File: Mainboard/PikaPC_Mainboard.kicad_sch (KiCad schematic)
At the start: 60 parts, among them J1 Conn_02x20_Odd_Even, J10 Conn_01x08, J11 Conn_01x08, J12 Conn_01x08, J13 Conn_01x08, J14 Conn_01x08, J15 Conn_01x08, J16 Conn_01x08, J17 Conn_01x08, J18 Conn_01x10, J19 Conn_02x05_Odd_Even, J2 Conn_02x20_Odd_Even, J3 Conn_02x20_Odd_Even, J4 Conn_02x20_Odd_Even, J5 Conn_01x18, J6 Conn_01x18, J7 Conn_01x18, J8 Conn_01x18, J9 Conn_01x08, SW1 SW_Push_DPDT, SW2 SW_Push, U1 PPC403GA, U10 74LVC245, U11 74LVC245, U12 GD75232N, U13 74LVC125, U14 MCP120-315GI/TO, U2 TE-822021-4, U3 SST39VF010, U4 74HCT244, U5 74HCT244, U6 74HCT244, U7 74LVC245, U8 74HCT32, U9 74LVC245, Y1 25M, Y2 7M3728

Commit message: Change from 72-pin SIMM to SRAM
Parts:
- removed J5, J6, J7, J8: Conn_01x18, Connector_PinHeader_2.54mm:PinHeader_1x18_P2.54mm_Vertical, symbol Connector_Generic:Conn_01x18
- removed U10, U11, U7, U9: 74LVC245, Package_DIP:DIP-20_W7.62mm_Socket, symbol 74xx:74HC245
- removed U2: TE-822021-4, PikaPC:SIMM72, symbol PikaPC:SIMM72
- removed U4, U5, U6: 74HCT244, Package_DIP:DIP-20_W7.62mm_Socket, symbol 74xx:74HCT244
- removed U8: 74HCT32, Package_DIP:DIP-14_W7.62mm_Socket, symbol 74xx:74LS32
- added C17, C18: 100nF, Capacitor_THT:C_Disc_D3.0mm_W2.0mm_P2.50mm, symbol Device:C_Small_US
- added U15, U16: AS6C4008-55PCN, Package_DIP:DIP-32_W15.24mm, symbol Memory_RAM:AS6C4008-55PCN
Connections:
- net +3.3V: now also C17.1, C18.1, U15.32 (VCC), U16.32 (VCC)
- net A1: now also U15.12 (A0), U16.12 (A0)
- net A10: now also U15.26 (A9), U16.26 (A9)
- net A11: now also U15.23 (A10), U16.23 (A10)
- net A12: now also U15.25 (A11), U16.25 (A11)
- net A13: now also U15.4 (A12), U16.4 (A12)
- net A14: now also U15.28 (A13), U16.28 (A13)
- net A15: now also U15.3 (A14), U16.3 (A14)
- net A16: now also U15.31 (A15), U16.31 (A15)
- net A17: now also U15.2 (A16), U16.2 (A16)
- net A18: now also U15.30 (A17), U16.30 (A17)
- net A19: now also U15.1 (A18), U16.1 (A18)
- net A2: now also U15.11 (A1), U16.11 (A1)
- net A26: no longer U1.123 (~{WBE1}/A5)
- net A27: no longer U1.122 (~{WBE0}/A4)
- net A3: now also U15.10 (A2), U16.10 (A2)
- net A4: now also U15.9 (A3), U16.9 (A3)
- net A5: now also U15.8 (A4), U16.8 (A4)
- net A6: now also U15.7 (A5), U16.7 (A5)
- net A7: now also U15.6 (A6), U16.6 (A6)
- net A8: now also U15.5 (A7), U16.5 (A7)
- net A9: now also U15.27 (A8), U16.27 (A8)
- net D16: now also U15.13 (DQ0)
- net D17: now also U15.14 (DQ1)
- net D18: now also U15.15 (DQ2)
- net D19: now also U15.17 (DQ3)
- net D20: now also U15.18 (DQ4)
- net D21: now also U15.19 (DQ5)
- net D22: now also U15.20 (DQ6)
- net D23: now also U15.21 (DQ7)
- net D24: now also U16.13 (DQ0)
- net D25: now also U16.14 (DQ1)
- net D26: now also U16.15 (DQ2)
- net D27: now also U16.17 (DQ3)
- net D28: now also U16.18 (DQ4)
- net D29: now also U16.19 (DQ5)
- net D30: now also U16.20 (DQ6)
- net D31: now also U16.21 (DQ7)
- net GND: now also C17.2, C18.2, U15.16 (VSS), U16.16 (VSS)
- net ~{CS1}: now also U15.22 (CE#), U16.22 (CE#)
- net ~{OE}: now also U15.24 (OE#), U16.24 (OE#)
- new net ~{WBE0}: U1.122 (~{WBE0}/A4), U16.29 (WE#)
- new net ~{WBE1}: U1.123 (~{WBE1}/A5), U15.29 (WE#)
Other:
- moved on the sheet: C13, C14, U13E, U3

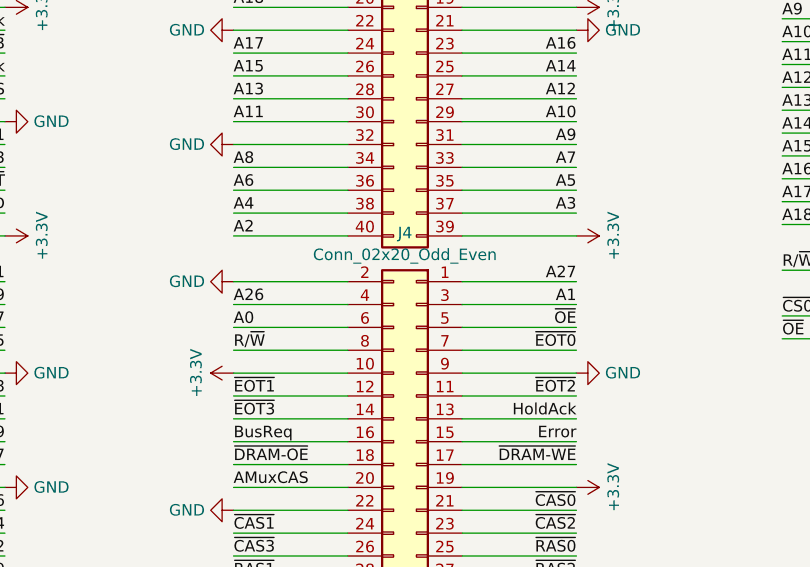
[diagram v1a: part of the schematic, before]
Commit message: Rename write strobes
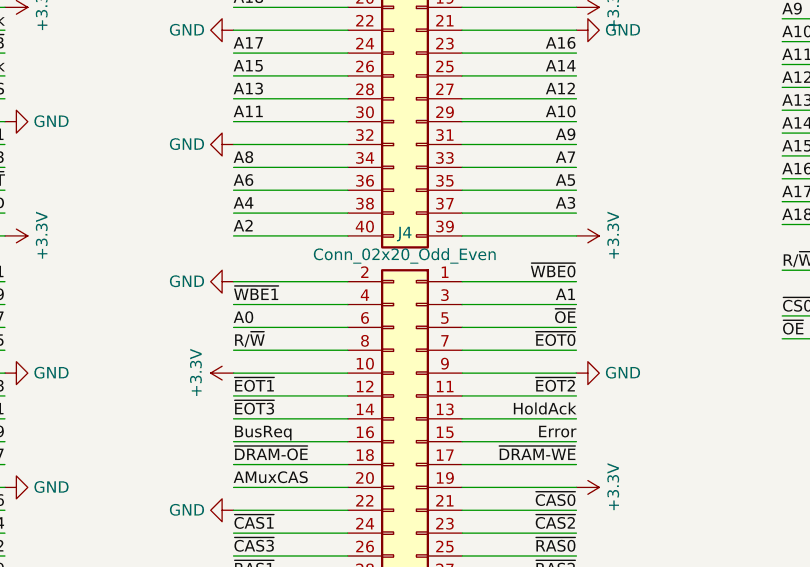
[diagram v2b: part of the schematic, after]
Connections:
- net A26 is gone; now on net ~{WBE1}: J4.4 (Pin_4)
- net A27 is gone; now on net ~{WBE0}: J4.1 (Pin_1)
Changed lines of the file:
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@@
 		)
 	)
-	(label "A26"
+	(label "~{WBE1}"
 		(at 292.1 81.28 0)
 		(effects
@@
 		)
 	)
-	(label "A27"
+	(label "~{WBE0}"
 		(at 330.2 78.74 180)
 		(effects

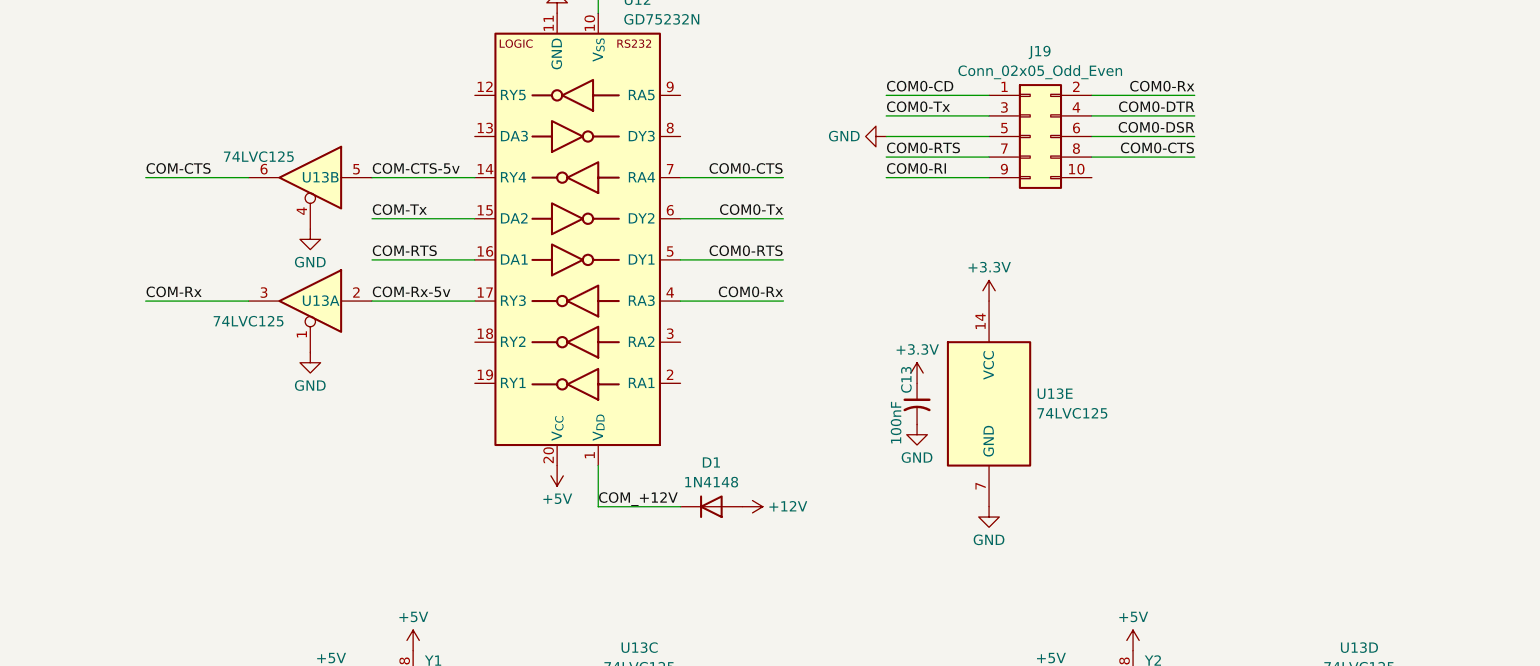
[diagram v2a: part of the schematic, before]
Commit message: use 5V signalling for Rx & CTS
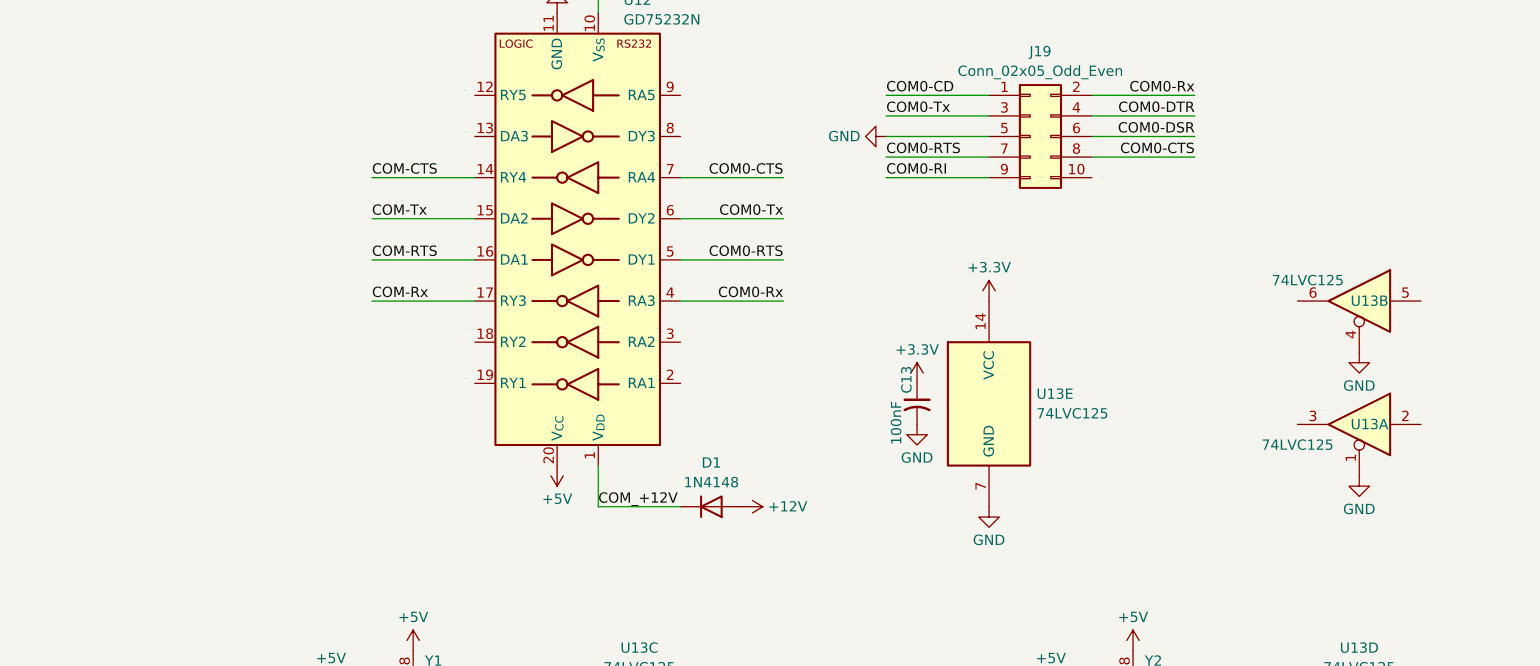
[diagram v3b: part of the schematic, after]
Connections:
- net COM-CTS: now also U12.14 (RY4); no longer U13.6
- net COM-Rx: now also U12.17 (RY3); no longer U13.3
- net COM-CTS-5v: no longer names the net of U13.5
- net COM-CTS-5v: no longer U12.14 (RY4)
- net COM-Rx-5v: no longer names the net of U13.2
- net COM-Rx-5v: no longer U12.17 (RY3)
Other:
- moved on the sheet: U13A, U13B
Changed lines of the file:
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@@
 	(wire
 		(pts
-			(xy 457.2 -101.6) (xy 469.9 -101.6)
-		)
-		(stroke
-			(width 0)
-			(type default)
-		)
-	)
-	(wire
-		(pts
 			(xy 495.3 44.45) (xy 482.6 44.45)
 		)
@@
 	(wire
 		(pts
-			(xy 457.2 -116.84) (xy 469.9 -116.84)
-		)
-		(stroke
-			(width 0)
-			(type default)
-		)
-	)
-	(wire
-		(pts
 			(xy 149.86 228.6) (xy 152.4 228.6)
 		)
@@
 	(wire
 		(pts
-			(xy 441.96 -101.6) (xy 429.26 -101.6)
+			(xy 469.9 -101.6) (xy 457.2 -101.6)
 		)
 		(stroke
@@
 	(wire
 		(pts
-			(xy 441.96 -116.84) (xy 429.26 -116.84)
+			(xy 469.9 -116.84) (xy 457.2 -116.84)
 		)
 		(stroke
@@
 		)
 	)
-	(label "COM-CTS-5v"
-		(at 457.2 -116.84 0)
-		(effects
-			(font
-				(size 1.27 1.27)
-			)
-			(justify left bottom)
-		)
-	)
 	(label "BusReq"
 		(at 205.74 55.88 180)
@@
 		)
 	)
-	(label "COM-Rx-5v"
-		(at 457.2 -101.6 0)
-		(effects
-			(font
-				(size 1.27 1.27)
-			)
-			(justify left bottom)
-		)
-	)
 	(label "A1"
 		(at 330.2 81.28 180)
@@
 	)
 	(label "COM-Rx"
-		(at 429.26 -101.6 0)
+		(at 457.2 -101.6 0)
 		(effects
 			(font
@@
 	)
 	(label "COM-CTS"
-		(at 429.26 -116.84 0)
+		(at 457.2 -116.84 0)
 		(effects
 			(font
@@
 	(symbol
 		(lib_id "power:GND")
-		(at 449.58 -110.49 0)
+		(at 579.12 -95.25 0)
 		(unit 1)
 		(exclude_from_sim no)
@@
 		(dnp no)
 		(property "Reference" "#PWR069"
-			(at 449.58 -104.14 0)
+			(at 579.12 -88.9 0)
 			(effects
 				(font
@@
 		)
 		(property "Value" "GND"
-			(at 449.58 -106.3569 0)
+			(at 579.12 -91.1169 0)
 			(effects
 				(font
@@
 		)
 		(property "Footprint" ""
-			(at 449.58 -110.49 0)
+			(at 579.12 -95.25 0)
 			(effects
 				(font
@@
 		)
 		(property "Datasheet" ""
-			(at 449.58 -110.49 0)
+			(at 579.12 -95.25 0)
 			(effects
 				(font
@@
 		)
 		(property "Description" "Power symbol creates a global label with name \"GND\" , ground"
-			(at 449.58 -110.49 0)
+			(at 579.12 -95.25 0)
 			(effects
 				(font
@@
 	(symbol
 		(lib_id "74xx:74LVC125")
-		(at 449.58 -116.84 0)
+		(at 579.12 -101.6 0)
 		(mirror y)
 		(unit 2)
@@
 		(dnp no)
 		(property "Reference" "U13"
-			(at 450.85 -116.84 0)
+			(at 580.39 -101.6 0)
 			(effects
 				(font
@@
 		)
 		(property "Value" "74LVC125"
-			(at 443.23 -119.38 0)
+			(at 572.77 -104.14 0)
 			(effects
 				(font
@@
 		)
 		(property "Footprint" "Package_DIP:DIP-14_W7.62mm_Socket"
-			(at 449.58 -116.84 0)
+			(at 579.12 -101.6 0)
 			(effects
 				(font
@@
 		)
 		(property "Datasheet" "http://www.ti.com/lit/gpn/sn74LVC125"
-			(at 449.58 -116.84 0)
+			(at 579.12 -101.6 0)
 			(effects
 				(font
@@
 		)
 		(property "Description" "Quad buffer 3-State outputs"
-			(at 449.58 -116.84 0)
+			(at 579.12 -101.6 0)
 			(effects
 				(font
@@
 	(symbol
 		(lib_id "74xx:74LVC125")
-		(at 449.58 -101.6 0)
+		(at 579.12 -86.36 0)
 		(mirror y)
 		(unit 1)
@@
 		(dnp no)
 		(property "Reference" "U13"
-			(at 450.85 -101.6 0)
+			(at 580.39 -86.36 0)
 			(effects
 				(font
@@
 		)
 		(property "Value" "74LVC125"
-			(at 441.96 -99.06 0)
+			(at 571.5 -83.82 0)
 			(effects
 				(font
@@
 		)
 		(property "Footprint" "Package_DIP:DIP-14_W7.62mm_Socket"
-			(at 449.58 -101.6 0)
+			(at 579.12 -86.36 0)
 			(effects
 				(font
@@
 		)
 		(property "Datasheet" "http://www.ti.com/lit/gpn/sn74LVC125"
-			(at 449.58 -101.6 0)
+			(at 579.12 -86.36 0)
 			(effects
 				(font
@@
 		)
 		(property "Description" "Quad buffer 3-State outputs"
-			(at 449.58 -101.6 0)
+			(at 579.12 -86.36 0)
 			(effects
 				(font
@@
 	(symbol
 		(lib_id "power:GND")
-		(at 449.58 -95.25 0)
+		(at 579.12 -80.01 0)
 		(unit 1)
 		(exclude_from_sim no)
@@
 		(fields_autoplaced yes)
 		(property "Reference" "#PWR067"
-			(at 449.58 -88.9 0)
+			(at 579.12 -73.66 0)
 			(effects
 				(font
@@
 		)
 		(property "Value" "GND"
-			(at 449.58 -91.1169 0)
+			(at 579.12 -75.8769 0)
 			(effects
 				(font
@@
 		)
 		(property "Footprint" ""
-			(at 449.58 -95.25 0)
+			(at 579.12 -80.01 0)
 			(effects
 				(font
@@
 		)
 		(property "Datasheet" ""
-			(at 449.58 -95.25 0)
+			(at 579.12 -80.01 0)
 			(effects
 				(font
@@
 		)
 		(property "Description" "Power symbol creates a global label with name \"GND\" , ground"
-			(at 449.58 -95.25 0)
+			(at 579.12 -80.01 0)
 			(effects
 				(font

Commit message: Add 8042 PS/2 Keyboard/Mouse controller
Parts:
- added C19, C20, C21, C22: 47p, Capacitor_THT:C_Disc_D7.5mm_W5.0mm_P7.50mm, symbol Device:C_Small_US
- added J20: Conn_02x05_Odd_Even, Connector_PinHeader_2.54mm:PinHeader_2x05_P2.54mm_Vertical, symbol Connector_Generic:Conn_02x05_Odd_Even
- added J5, J6, J7, J8: Conn_02x05_Odd_Even, Connector_PinHeader_2.54mm:PinHeader_2x05_P2.54mm_Horizontal, symbol Connector_Generic:Conn_02x05_Odd_Even
- added Q1, Q2, Q3, Q4: PN2222A, Package_TO_SOT_THT:TO-92_Inline, symbol Transistor_BJT:PN2222A
- added R10, R3, R4, R6, R7: 4k7, Resistor_THT:R_Axial_DIN0204_L3.6mm_D1.6mm_P2.54mm_Vertical, symbol Device:R_Small_US
- added R2, R5, R8, R9: 10k, Resistor_THT:R_Axial_DIN0204_L3.6mm_D1.6mm_P2.54mm_Vertical, symbol Device:R_Small_US
- added U2, U4, U5, U6: SN74LVC245A, Package_DIP:DIP-20_W7.62mm_Socket, symbol 74xx:74LS245
- added U7: 8042 PS/2, symbol MCU_Intel:8040
- added U8: ATF22V10C, symbol Logic_Programmable:PAL20RS10
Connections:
- net +3.3V: now also U2.20 (VCC), U4.20 (VCC), U5.20 (VCC), U6.20 (VCC)
- net +5V: now also R10.2, R2.2, R5.2, R8.2, R9.2, U7.25 (NC), U7.26 (TEST), U7.40 (VCC), U7.5 (~{SS}), U8.24 (VCC)
- net D0: now also U5.18 (B0)
- net D1: now also U5.17 (B1)
- net D10: now also U6.16 (B2)
- net D11: now also U6.15 (B3)
- net D12: now also U6.14 (B4)
- net D13: now also U6.13 (B5)
- net D14: now also U6.12 (B6)
- net D15: now also U6.11 (B7)
- net D16: now also U2.18 (B0)
- net D17: now also U2.17 (B1)
- net D18: now also U2.16 (B2)
- net D19: now also U2.15 (B3)
- net D2: now also U5.16 (B2)
- net D20: now also U2.14 (B4)
- net D21: now also U2.13 (B5)
- net D22: now also U2.12 (B6)
- net D23: now also U2.11 (B7)
- net D24: now also U4.18 (B0)
- net D25: now also U4.17 (B1)
- net D26: now also U4.16 (B2)
- net D27: now also U4.15 (B3)
- net D28: now also U4.14 (B4)
- net D29: now also U4.13 (B5)
- net D3: now also U5.15 (B3)
- net D30: now also U4.12 (B6)
- net D31: now also U4.11 (B7)
- net D4: now also U5.14 (B4)
- net D5: now also U5.13 (B5)
- net D6: now also U5.12 (B6)
- net D7: now also U5.11 (B7)
- net D8: now also U6.18 (B0)
- net D9: now also U6.17 (B1)
- net GND: now also C19.2, C20.2, C21.2, C22.2, J20.9 (Pin_9), J5.1 (Pin_1), J5.2 (Pin_2), J6.1 (Pin_1), J6.2 (Pin_2), J7.1 (Pin_1), J7.2 (Pin_2), J8.1 (Pin_1), J8.2 (Pin_2), Q1.1 (E), Q2.1 (E), Q3.1 (E), Q4.1 (E), U2.10 (GND), U4.10 (GND), U5.10 (GND), U6.10 (GND), U7.2 (X1), U7.20 (GND), U7.7 (EA), U8.12 (GND)
- net Ready: now also J20.2 (Pin_2), U8.22 (IO22)
- net R/~{W}: now also J20.4 (Pin_4), U2.1 (A->B), U4.1 (A->B), U5.1 (A->B), U6.1 (A->B), U7.10 (~{WR})
- net SerClk-5v: now also U7.3 (X2)
- net SysClk-5v: now also U8.1 (CLK)
- net ~{CS2}: now also J20.8 (Pin_8), U8.2 (I2)
- net ~{CS3}: now also J20.6 (Pin_6), U8.3 (I3)
- net ~{OE}: now also U7.8 (~{RD}), U8.6 (I6)
- net ~{RAS0}: no longer U1.146 (~{CS7}/~{RAS0})
- net ~{RAS1}: no longer U1.147 (~{CS6}/~{RAS1})
- net ~{RAS2}: no longer U1.148 (~{CS5}/~{RAS2})
- net ~{RAS3}: no longer U1.151 (~{CS4}/~{RAS3})
- net ~{Reset}: now also U7.4 (~{RESET})
- net ~{WBE0}: now also U8.7 (I7)
- net ~{WBE1}: now also U8.8 (I8)
- net A0 renamed A0/~{WBE3}
- net A0/~{WBE3}: now also U7.9 (A0), U8.10 (I10)
- net A1 renamed A1/~{WBE2}
- net A1/~{WBE2}: now also U8.9 (I9)
- new net: Q3.2 (B), R6.2
- new net: R6.1, U7.37 (KBCO)
- new net: Q4.2 (B), R7.2
- new net: Q1.2 (B), R3.2
- new net: R4.1, U7.24 (MSCO)
- new net: Q2.2 (B), R4.2
- new net: R7.1, U7.38 (KBDO)
- new net: R3.1, U7.23 (MSDO)
- new net: R10.1, U7.34 (~{KBD-INH})
- new net KCLK: C21.1, Q3.3 (C), R8.1, U7.1 (T0)
- new net KDAT: C22.1, Q4.3 (C), R9.1, U7.27 (KBDI)
- new net MCLK: C20.1, Q2.3 (C), R5.1, U7.39 (KBDI/MSCI)
- new net MDAT: C19.1, Q1.3 (C), R2.1, U7.28 (MSDI)
- new net PD0: U5.2 (A0)
- new net PD1: U5.3 (A1)
- new net PD10: U6.4 (A2)
- new net PD11: U6.5 (A3)
- new net PD12: U6.6 (A4)
- new net PD13: U6.7 (A5)
- new net PD14: U6.8 (A6)
- new net PD15: U6.9 (A7)
- new net PD16: U2.2 (A0)
- new net PD17: U2.3 (A1)
- new net PD18: U2.4 (A2)
- new net PD19: U2.5 (A3)
- new net PD2: U5.4 (A2)
- new net PD20: U2.6 (A4)
- new net PD21: U2.7 (A5)
- new net PD22: U2.8 (A6)
- new net PD23: U2.9 (A7)
- new net PD24: U4.2 (A0), U7.12 (D0)
- new net PD25: U4.3 (A1), U7.13 (D1)
- new net PD26: U4.4 (A2), U7.14 (D2)
- new net PD27: U4.5 (A3), U7.15 (D3)
- new net PD28: U4.6 (A4), U7.16 (D4)
- new net PD29: U4.7 (A5), U7.17 (D5)
- new net PD3: U5.5 (A3)
- new net PD30: U4.8 (A6), U7.18 (D6)
- new net PD31: U4.9 (A7), U7.19 (D7)
- new net PD4: U5.6 (A4)
- new net PD5: U5.7 (A5)
- new net PD6: U5.8 (A6)
- new net PD7: U5.9 (A7)
- new net PD8: U6.2 (A0)
- new net PD9: U6.3 (A1)
- new net VA0: J5.9 (Pin_9)
- new net VA1: J5.7 (Pin_7)
- new net VA10: J7.5 (Pin_5)
- new net VA11: J7.3 (Pin_3)
- new net VA12: J8.9 (Pin_9)
- new net VA13: J8.7 (Pin_7)
- new net VA14: J8.5 (Pin_5)
- new net VA15: J8.3 (Pin_3)
- new net VA2: J5.5 (Pin_5)
- new net VA3: J5.3 (Pin_3)
- new net VA4: J6.9 (Pin_9)
- new net VA5: J6.7 (Pin_7)
- new net VA6: J6.5 (Pin_5)
- new net VA7: J6.3 (Pin_3)
- new net VA8: J7.9 (Pin_9)
- new net VA9: J7.7 (Pin_7)
- new net VD0: J5.10 (Pin_10)
- new net VD1: J5.8 (Pin_8)
- new net VD10: J7.6 (Pin_6)
- new net VD11: J7.4 (Pin_4)
- new net VD12: J8.10 (Pin_10)
- new net VD13: J8.8 (Pin_8)
- new net VD14: J8.6 (Pin_6)
- new net VD15: J8.4 (Pin_4)
- new net VD2: J5.6 (Pin_6)
- new net VD3: J5.4 (Pin_4)
- new net VD4: J6.10 (Pin_10)
- new net VD5: J6.8 (Pin_8)
- new net VD6: J6.6 (Pin_6)
- new net VD7: J6.4 (Pin_4)
- new net VD8: J7.10 (Pin_10)
- new net VD9: J7.8 (Pin_8)
- new net ~{CS4}: U1.151 (~{CS4}/~{RAS3}), U8.4 (I4)
- new net ~{CS5}: U1.148 (~{CS5}/~{RAS2}), U7.6 (~{CS}), U8.5 (I5)
- new net ~{CS6}: U1.147 (~{CS6}/~{RAS1})
- new net ~{CS7}: U1.146 (~{CS7}/~{RAS0})
- new net ~{PDBEN}: U2.19 (CE), U4.19 (CE), U5.19 (CE), U6.19 (CE), U8.23 (IO23)
- new net ~{VCABEN}: J20.1 (Pin_1)
- new net ~{VCDBEN}: J20.3 (Pin_3)
- new net ~{VID-ADS}: U8.15 (IO15)
- new net ~{VID-RDYIN}: U8.21 (IO21)
- new net ~{VID-SBE0}: U8.20 (IO20)
- new net ~{VID-SBE1}: U8.19 (IO19)
- new net ~{VID-SBE2}: U8.18 (IO18)
- new net ~{VID-SBE3}: U8.17 (IO17)
- new net ~{VID-SRDYn}: U8.11 (I11)
- new net ~{VOE}: J20.5 (Pin_5)
- new net ~{VWE}: J20.7 (Pin_7)
- no-connect marks 0 -> 1
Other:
- note added: "ADS-Q0"

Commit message: Keyboard/Mouse controller use '04/'07
- use tried & true 7404+7407 instead of discrete transistors
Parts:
- removed J20: Conn_02x05_Odd_Even, Connector_PinHeader_2.54mm:PinHeader_2x05_P2.54mm_Vertical, symbol Connector_Generic:Conn_02x05_Odd_Even
- removed J5, J6, J7, J8: Conn_02x05_Odd_Even, Connector_PinHeader_2.54mm:PinHeader_2x05_P2.54mm_Horizontal, symbol Connector_Generic:Conn_02x05_Odd_Even
- removed Q1, Q2, Q3, Q4: PN2222A, Package_TO_SOT_THT:TO-92_Inline, symbol Transistor_BJT:PN2222A
- removed R3, R4, R6, R7: 4k7, Resistor_THT:R_Axial_DIN0204_L3.6mm_D1.6mm_P2.54mm_Vertical, symbol Device:R_Small_US
- added C23: 100nF, Capacitor_THT:C_Disc_D3.0mm_W2.0mm_P2.50mm, symbol Device:C_Small_US
- added J5: DIN41612_03x32_C_Split, Connector_DIN:DIN41612_C_3x32_Female_Vertical_THT, symbol Connector:DIN41612_03x32_C_Split
- added J6, J7: Mini-DIN-6, Connector_PinHeader_2.54mm:PinHeader_2x03_P2.54mm_Vertical, symbol Connector:Mini-DIN-6
- added U10: 74LS07, Package_DIP:DIP-14_W7.62mm_Socket, symbol 74xx:74LS07
- added U9: 74LS04, Package_DIP:DIP-14_W7.62mm_Socket, symbol 74xx:74LS04
- added Y3: 14M31818, Oscillator:Oscillator_DIP-8, symbol Oscillator:CXO_DIP8
- U7: footprint (none) -> Package_DIP:DIP-40_W15.24mm_Socket
- U8: footprint (none) -> Package_DIP:DIP-24_W7.62mm_Socket
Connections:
- net +5V: now also C23.1, J6.4, J7.4, U10.14 (VCC), U9.14 (VCC), Y3.8 (Vcc)
- net GND: now also C23.2, J6.3, J7.3, U10.7 (GND), U9.7 (GND), Y3.4 (GND)
- net KCLK: now also J6.5, U10.6
- net KDAT: now also J6.1, U10.8
- net MCLK: now also J7.5, U10.4
- net MDAT: now also J7.1, U10.2
- net at U7.37 (KBCO): now also U9.5
- net at U7.24 (MSCO): now also U9.3
- net at U7.38 (KBDO): now also U9.9
- net at U7.23 (MSDO): now also U9.1
- new net: U10.3, U9.4
- new net: U10.5, U9.6
- new net: U10.9, U9.8
- new net: U10.1, U9.2
- new net VidClk: Y3.5 (OUT)
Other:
- moved on the sheet: C15, C16, U13C, U13D, Y1, Y2
